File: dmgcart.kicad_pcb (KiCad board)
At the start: 2 copper layers, 51.4 x 61 mm, 62 parts, among them J1 GameBoy_Cartridge, J3 Micro_SD_Card, J4 Conn_ARM_JTAG_SWD_10, J5 47346-0001, Q1 2N7002, SW1 BOOT0, SW2 RESET, SW3 BOOT1, U1 STM32F429ZIT6, U2 IS42S16400J-7TL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

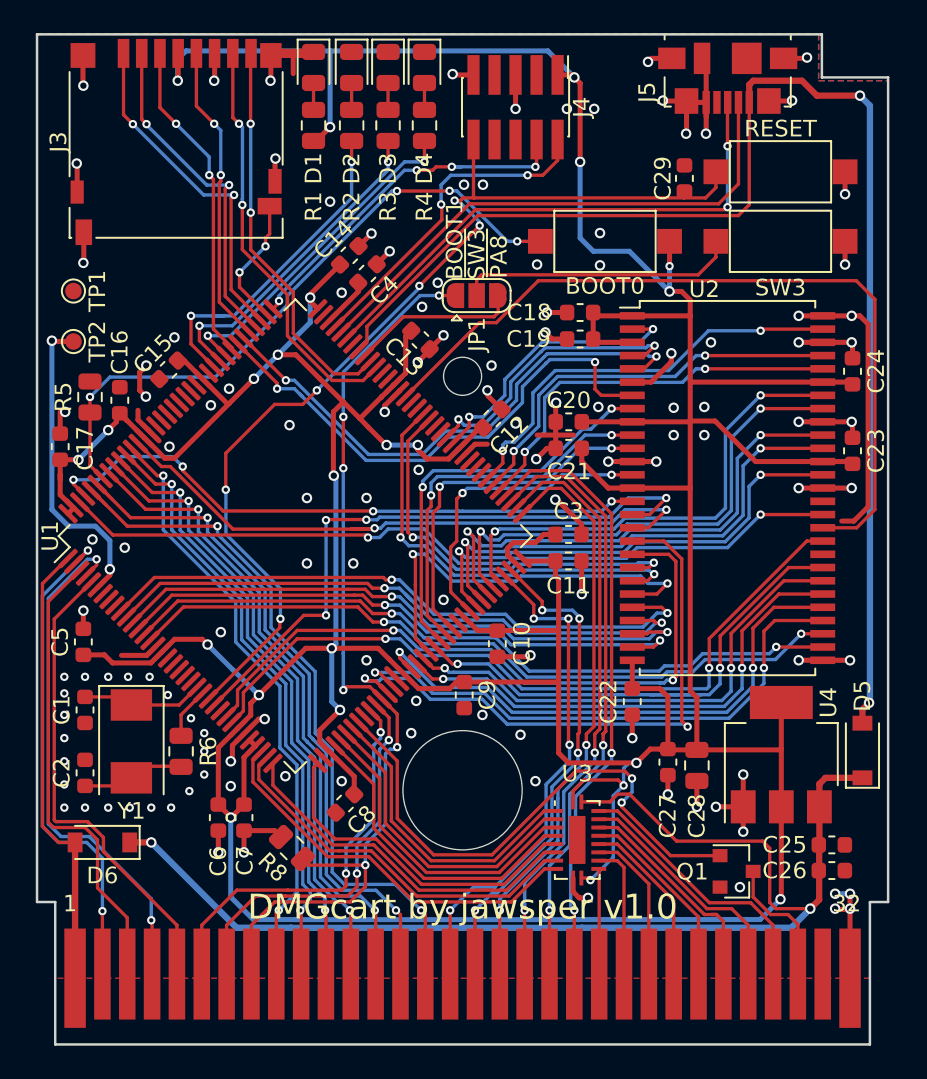
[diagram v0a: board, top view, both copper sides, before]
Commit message: Updated design files
* Moved components up so they shouldn't collide with the case.
* Rereferenced components so they are sorted by value.
* Added pad for 32k RTC oscillator.
* Several small tweaks to routing.
* Added component value list to back silkscreen.

* Added board renders
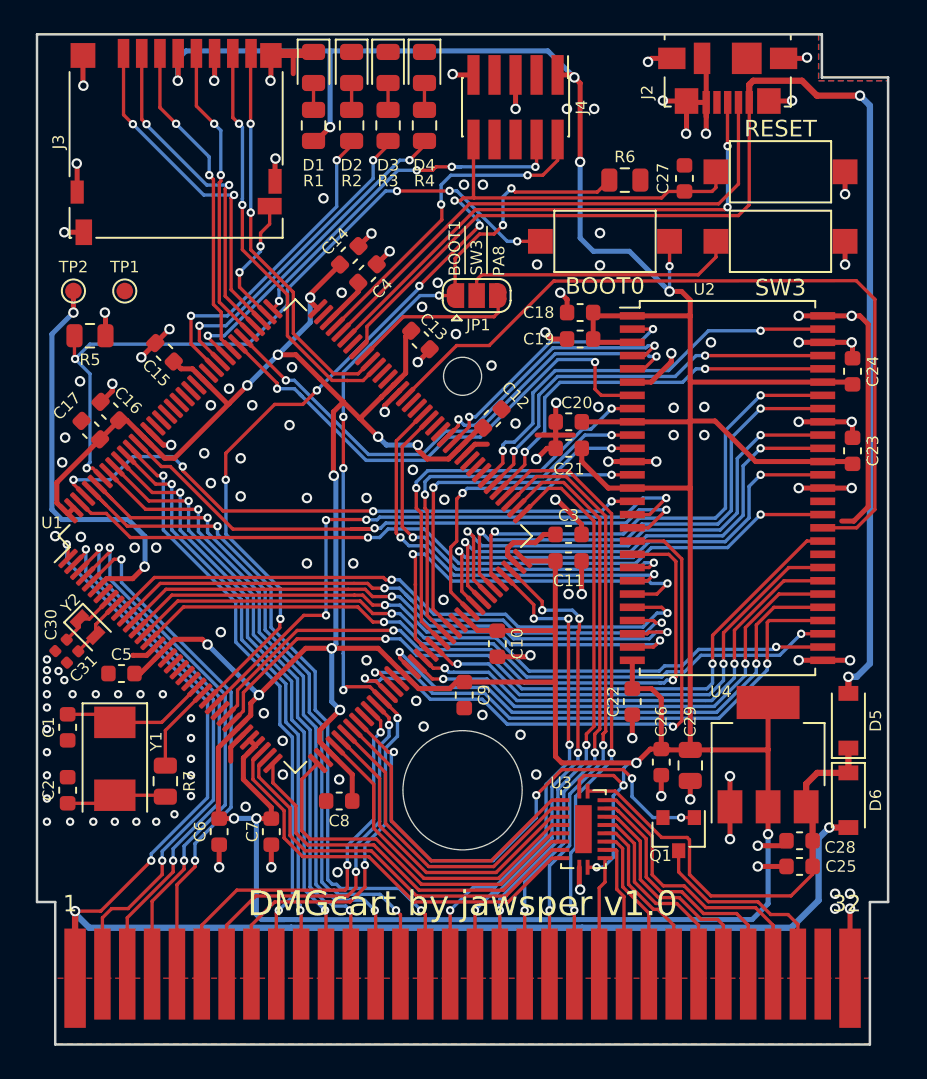
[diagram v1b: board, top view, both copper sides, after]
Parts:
- removed the C25 at (122.3, 92.0)
- added C28: 10u, Capacitor_SMD:C_0603_1608Metric, F.Cu at (120.3, 91.7)
- added C30: 3pF, Capacitor_SMD:C_0402_1005Metric, F.Cu at (75.8, 79.9)
- added C31: 3pF, Capacitor_SMD:C_0402_1005Metric, F.Cu at (76.5, 80.6)
- added Y2: 32.768 kHz, Crystal:Crystal_SMD_2012-2Pin_2.0x1.2mm, F.Cu at (77.3, 78.8)
- R1, R2, R3, R4: value 470 -> 470R
- R7: renamed from R6; value 10k -> 0R
- moved D6 45.1 mm to (123.3, 89.2), turned to 270 degrees
- moved R6 45.1 mm to (109.8, 51.8), turned to 0 degrees
- moved Q1 4.16 mm to (113.0, 91.3), turned to 270 degrees
- moved R5 3.70 mm to (77.5, 61.2), turned to 0 degrees
- moved TP1 3.10 mm to (79.6, 58.5)
- moved TP2 3.05 mm to (76.5, 58.5)
- moved C5 2.99 mm to (79.4, 81.6), turned to 0 degrees
- moved C17 2.10 mm to (77.5, 66.9), turned to 315 degrees
- moved R7 2.04 mm to (82.0, 88.1)
- moved D5 1.99 mm to (123.3, 84.5)
- moved C25 1.97 mm to (120.3, 93.2), turned to 0 degrees
- moved C7 1.86 mm to (88.5, 91.2)
- moved C2 1.48 mm to (76.2, 88.7)
- moved C1 1.48 mm to (76.2, 84.8)
- moved Y1 1.45 mm to (79.0, 86.8)
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- renumbered C26 to C25, C27 to C26, C29 to C27, C28 to C29, J5 to J2, R8 to R6
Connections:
- net Net-(J5-Pad4) renamed /USB_ID
- U1 pad 8: Net-(U1-Pad8) -> /OSC32_IN
- U1 pad 9: Net-(U1-Pad9) -> /OSC32_OUT
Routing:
- net /GB_VCC: track 27.6 -> 87.0 mm, vias 0 -> 4
- net +5V: track 73.0 -> 27.9 mm, vias 2 -> 0
- net /GB_A2-BOOT1: track 58.0 -> 68.6 mm, vias 6 -> 8
- net GND: track 137.6 -> 129.1 mm, vias 126 -> 144
- net /VBAT: track 19.0 -> 25.3 mm
- net /GB_NRST: track 7.93 -> 12.7 mm
- net /BOOT0: track 39.2 -> 43.9 mm, vias 4 -> 5
- net /GB_NWR: track 28.3 -> 32.9 mm, vias 0 -> 2
- net +3V3: track 364.1 -> 360.1 mm, vias 23 -> 22
- net /OSC32_IN: track 0.00 -> 3.85 mm
- net /OSC32_OUT: track 0.00 -> 3.74 mm
- net /RAM_A11: track 32.6 -> 29.5 mm
- net /GB_CLK: track 30.4 -> 33.4 mm
- net /GB_NCS: track 28.8 -> 31.5 mm, vias 0 -> 2
- net Net-(R7-Pad1): track 3.12 -> 5.31 mm
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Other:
- board text added: "22pF 2.2 uF 100 nF 10 uF 47 uF 3 pF 470 R 10k 0 R LED Schottky 2N7002 GND VBAT 8 MHz 32.768 kHz STM32F429ZIT IS42S16400J-7TL FXMA108BQX AMS1117-3.3"
- board text added: "C1-C2 C3-C4 C5-C27 C28 C29 C30-C31 R1-R4 R5-R6 R7 D1-D4 D5-D6 Q1 TP1 TP2 Y1 Y2 U1 U2 U3 U4"
- board text added: "DMGcart STM32F429 Game Boy flashcart Made in 2020 by jawsper Version 1.0"
- board text removed: "DMGcart a STM32F429 Game Boy flashcart Made in 2020 by jawsper Version 1.0"

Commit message: Fix #1: Tie /OE of U3 to PC5 instead of VCC.
This was an error, tying /OE to VCC actually disables the outputs
of U3. By tying it to a GPIO, it can be controlled by the MCU instead.

Additional changes:
* Some small tweaks on the PCB settings in KiCad (board thickness etc)
* Updated HTML BOM.
* Changed revision to v1.1
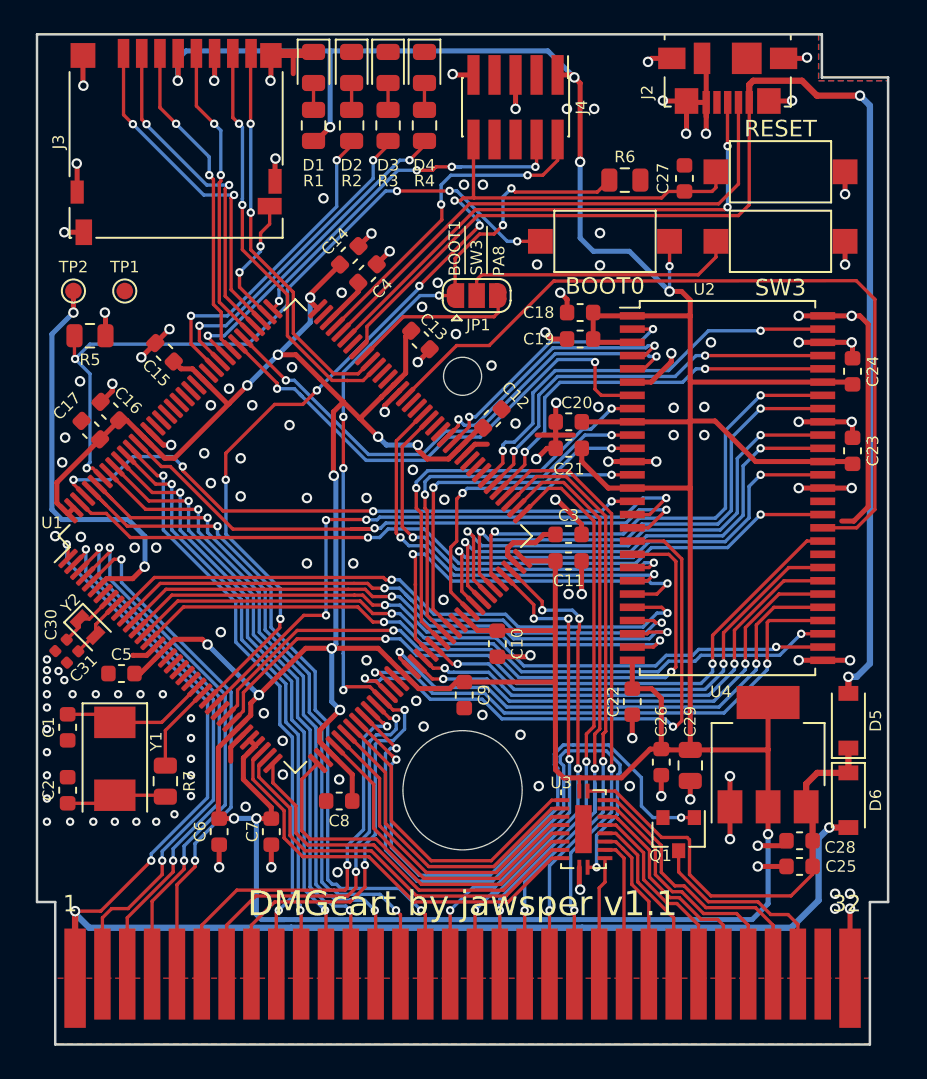
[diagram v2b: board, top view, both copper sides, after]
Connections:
- U1 pad 45: Net-(U1-Pad45) -> /LVL_SHIFT_OE
- U3 pad 11: +3V3 -> /LVL_SHIFT_OE
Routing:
- net /LVL_SHIFT_OE: track 0.00 -> 37.4 mm, vias 0 -> 2
- net +3V3: track 360.1 -> 350.1 mm, vias 22 -> 19
- net /DMG_RESET: track 31.3 -> 35.9 mm, vias 4 -> 2
- net /GB_A13: track 35.9 -> 37.7 mm
- net /GB_A2-BOOT1: track 68.6 -> 69.9 mm
- net /GB_A1: track 23.9 -> 25.0 mm
- net /GB_A0: track 24.5 -> 25.3 mm
- net /RAM_SDCKE0: track 45.1 -> 44.4 mm
- net /RAM_SDNE0: track 41.2 -> 40.6 mm
- net /RAM_A11: track 29.5 -> 28.9 mm
- net /RAM_A9: track 29.9 -> 29.3 mm
- net GND: vias 144 -> 145
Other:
- board text added: "DMGcart STM32F429 Game Boy flashcart Made in 2020 by jawsper Version 1.1"
- board text added: "DMGcart by jawsper v1.1"
- board text removed: "DMGcart STM32F429 Game Boy flashcart Made in 2020 by jawsper Version 1.0"
- board text removed: "DMGcart by jawsper v1.0"
